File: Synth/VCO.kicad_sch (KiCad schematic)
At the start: 0 parts

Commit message: added components
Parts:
- added U1: TL074, symbol Amplifier_Operational:TL074
- added U2: SN74LVC1G14DBV, Package_TO_SOT_SMD:SOT-23-5, symbol 74xGxx:SN74LVC1G14DBV

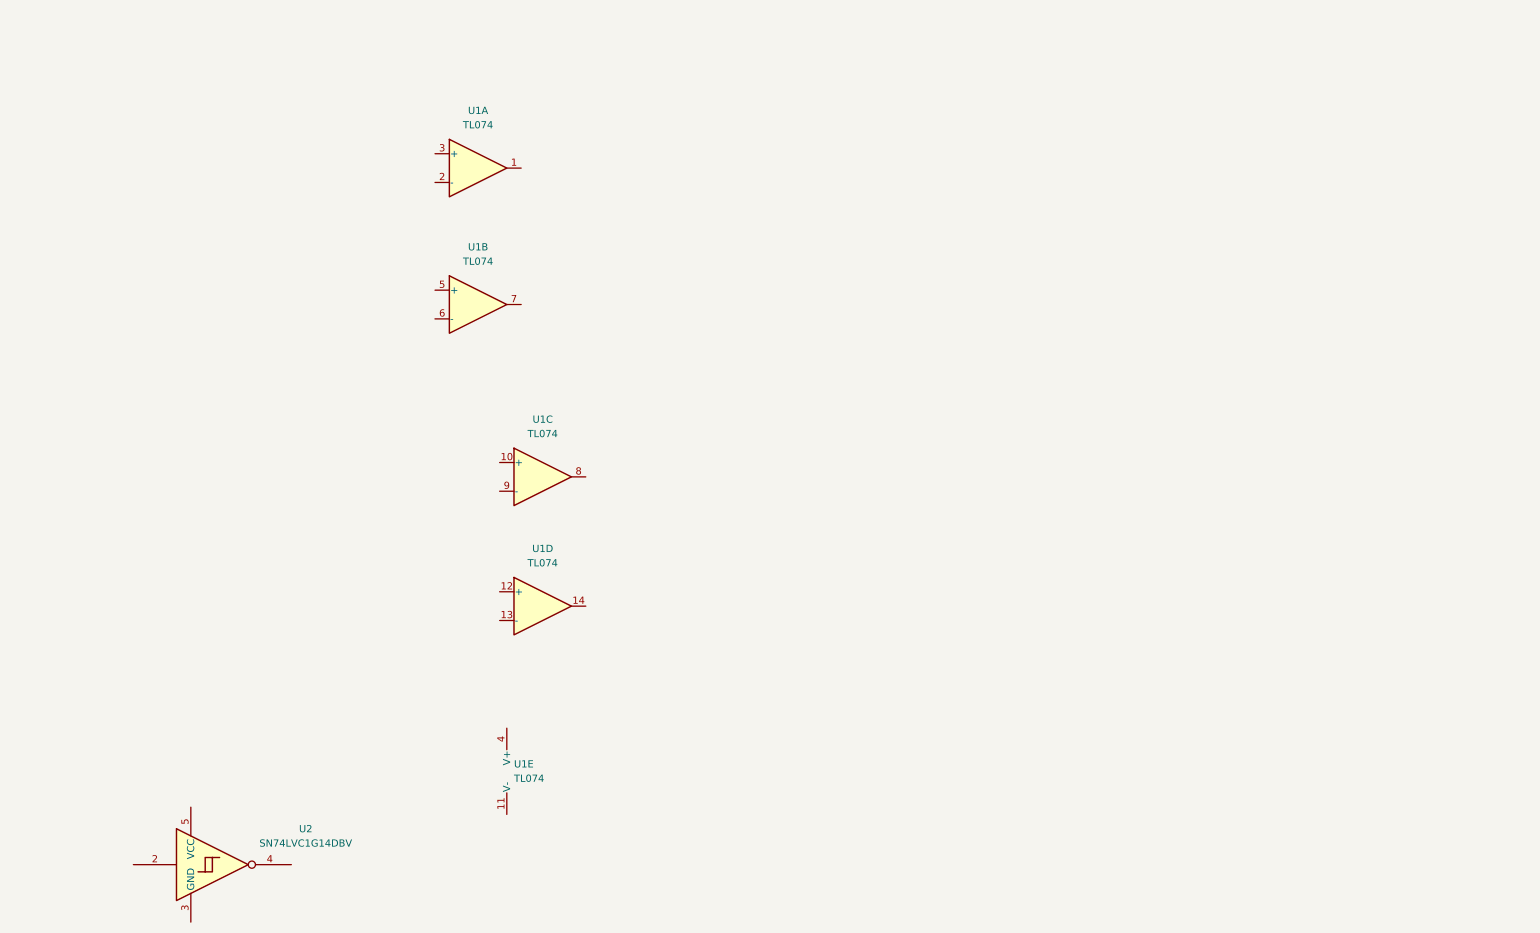
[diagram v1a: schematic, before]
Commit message: Update VCO schematic and add project backups
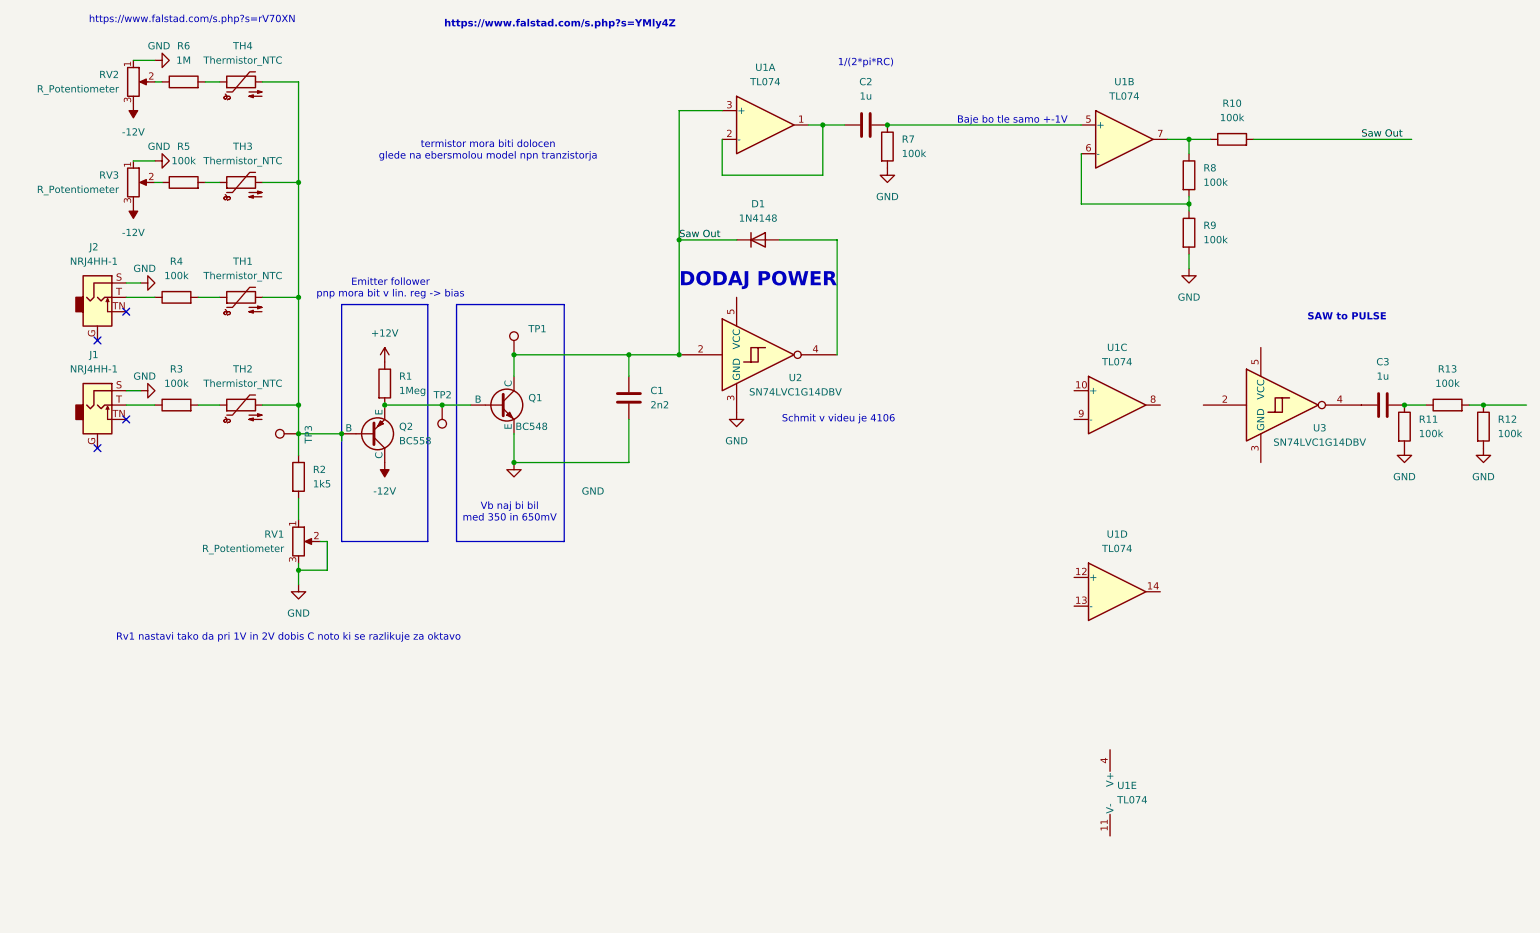
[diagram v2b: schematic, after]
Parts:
- added C1: 2n2, symbol Device:C
- added C2, C3: 1u, symbol Device:C
- added D1: 1N4148, Diode_THT:D_DO-35_SOD27_P7.62mm_Horizontal, symbol Diode:1N4148
- added J1, J2: NRJ4HH-1, Connector_Audio:Jack_3.5mm_CUI_SJ1-3524N_Horizontal, symbol Connector_Audio:NRJ4HH-1
- added Q1: BC548, symbol Simulation_SPICE:NPN
- added Q2: BC558, symbol Simulation_SPICE:PNP
- added R1: 1Meg, symbol Device:R
- added R10, R11, R12, R13, R3, R4, R5, R7, R8, R9: 100k, symbol Device:R
- added R2: 1k5, symbol Device:R
- added R6: 1M, symbol Device:R
- added RV1, RV2, RV3: R_Potentiometer, symbol Device:R_Potentiometer
- added TH1, TH2, TH3, TH4: Thermistor_NTC, symbol Device:Thermistor_NTC
- added TP1, TP2, TP3: TestPoint, symbol Connector:TestPoint
- added U3: SN74LVC1G14DBV, Package_TO_SOT_SMD:SOT-23-5, symbol 74xGxx:SN74LVC1G14DBV
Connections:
- net at U1.5 (+): now also C2.1, R7.1
- net at U1.6 (-): now also R8.2, R9.1
- net at U1.7: now also R10.1, R8.1
- net at U1.1: now also U1.2 (-), C2.2
- net Saw Out: now reaches U1.3 (+)
- net Saw Out: now also U2.2, C1.1, D1.1 (K), Q1.1 (C), R10.2, TP1.1
- net GND: now reaches U2.3 (GND)
- net GND: now also C1.2, J1.S, J2.S, Q1.3 (E), R11.2, R12.2, R7.2, R9.2, RV1.2, RV1.3, RV2.1, RV3.1
- net at U2.4: now also D1.2 (A)
- new net: R4.2, TH1.1
- new net: Q2.2 (B), R2.1, TH1.2, TH2.2, TH3.2, TH4.2, TP3.1
- new net: R5.1, RV3.2
- new net: R6.1, RV2.2
- new net: Q1.2 (B), Q2.3 (E), R1.2, TP2.1
- new net: J2.T, R4.1
- new net: R6.2, TH4.1
- new net: R2.2, RV1.1
- new net: C3.2, U3.4
- new net: R5.2, TH3.1
- new net: C3.1, R11.1, R13.1
- new net: R12.1, R13.2
- new net: R3.2, TH2.1
- new net: J1.T, R3.1
- new net +12V: R1.1
- new net -12V: Q2.1 (C), RV2.3, RV3.3
- no-connect marks 0 -> 4
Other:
- note added: "1/(2*pi*RC)"
- note added: "Baje bo tle samo +-1V"
- note added: "DODAJ POWER"
- note added: "Emitter follower pnp mora bit v lin. reg -> bias"
- note added: "Rv1 nastavi tako da pri 1V in 2V dobis C noto ki se razlikuje za oktavo"
- note added: "SAW to PULSE"
- note added: "Schmit v videu je 4106"
- note added: "Vb naj bi bil med 350 in 650mV"
- note added: "https://www.falstad.com/s.php?s=YMly4Z"
- note added: "https://www.falstad.com/s.php?s=rV70XN"
- note added: "termistor mora biti dolocen glede na ebersmolou model npn tranzistorja"
- moved on the sheet: U1A, U1B, U1C, U1D, U1E, U2
